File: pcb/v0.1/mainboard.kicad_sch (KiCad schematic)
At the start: 9 parts, among them J1 Conn_01x02_Pin, J2 TYPE_C_Receptacle, J3 Conn_01x04_Pin, U1 AP2112K-3.3TRG1

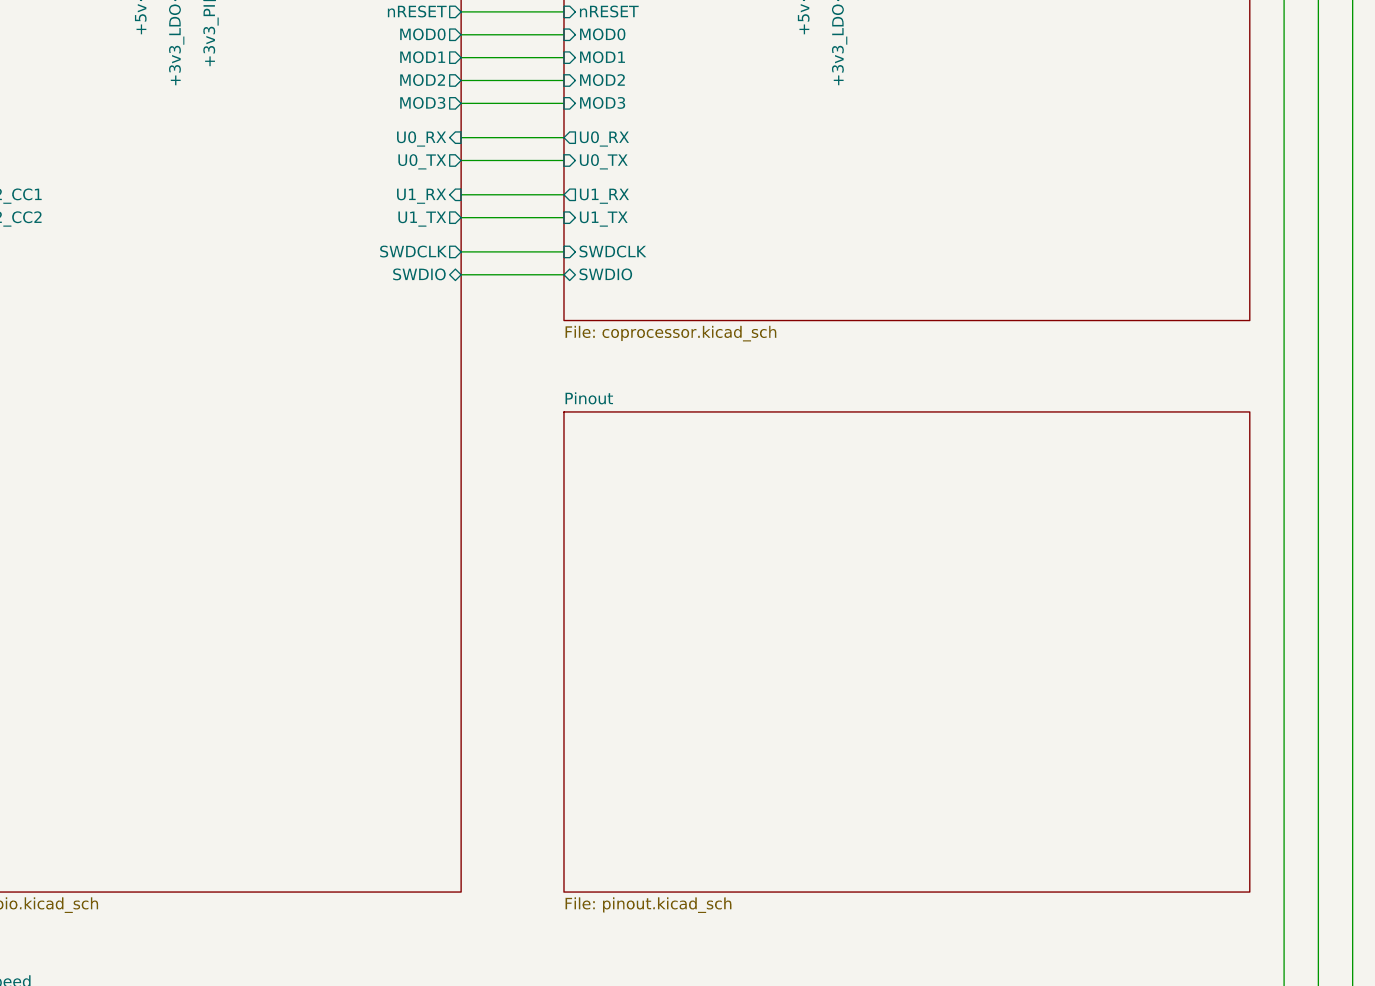
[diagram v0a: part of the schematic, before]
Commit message: Pinout for CM5 and co processor.
I've tried to make the pinout expose as many different protocols as
possible. Standard GPIO exists, but it was not a priority as I think its
more important to have protocols for the backpack.

The co processor also has 8 pins tied as input only. These are
technically I/O, but they have a resistor on them which may mess up some
output operations.
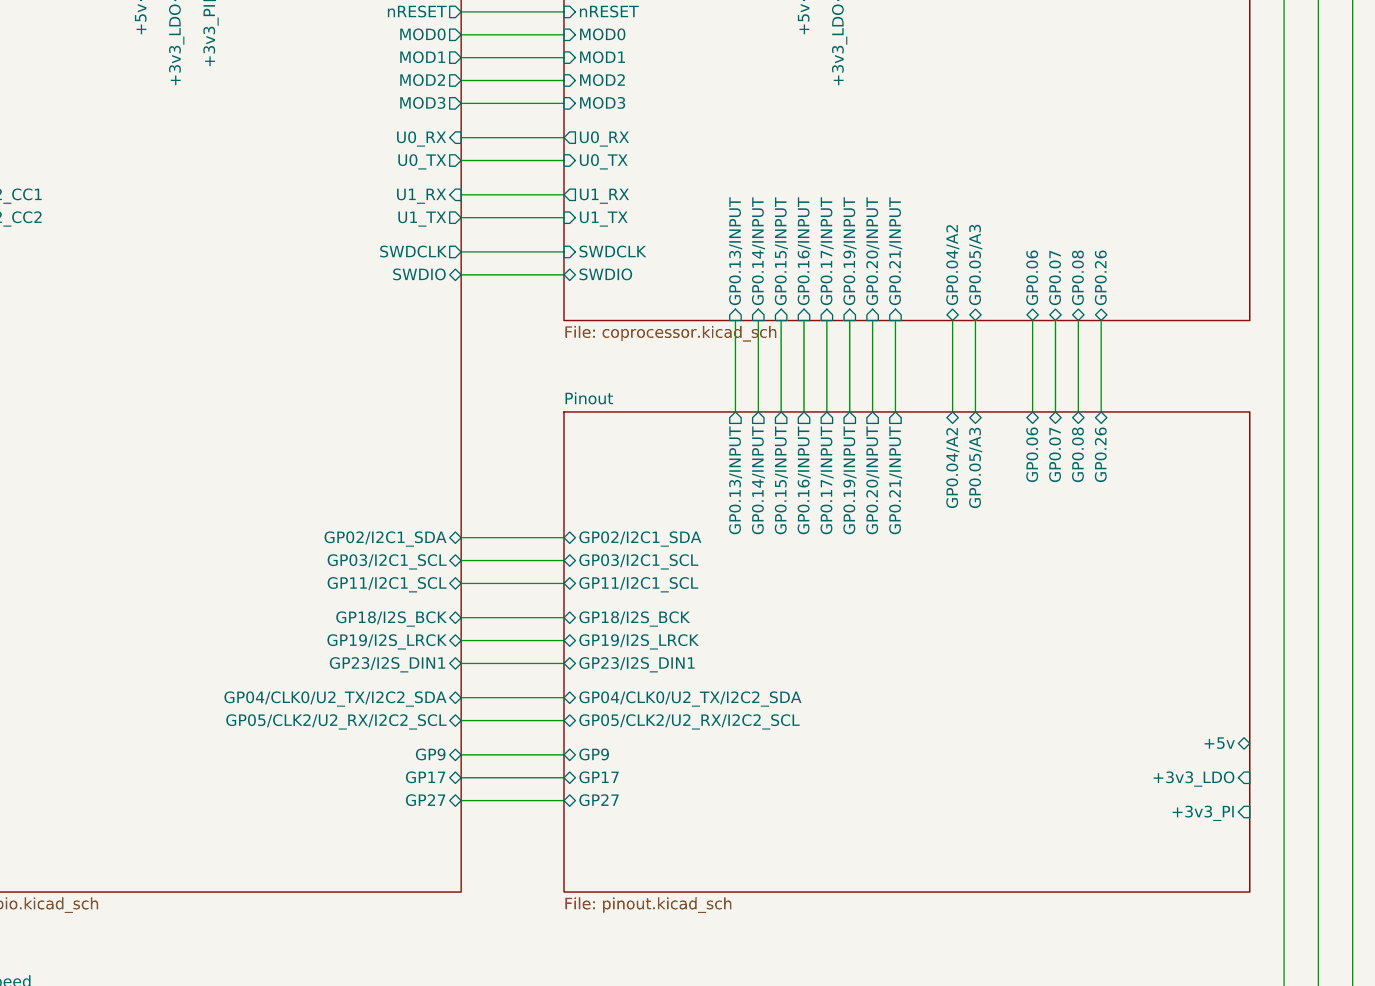
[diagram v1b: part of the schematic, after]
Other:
- sheet Co processor ports: added GP0.04/A2, GP0.05/A3, GP0.06, GP0.07, GP0.08, GP0.13/INPUT, GP0.14/INPUT, GP0.15/INPUT, GP0.16/INPUT, GP0.17/INPUT, GP0.19/INPUT, GP0.20/INPUT, GP0.21/INPUT, GP0.26; removed none
- sheet GPIO ports: added GP02/I2C1_SDA, GP03/I2C1_SCL, GP04/CLK0/U2_TX/I2C2_SDA, GP05/CLK2/U2_RX/I2C2_SCL, GP11/I2C1_SCL, GP17, GP18/I2S_BCK, GP19/I2S_LRCK, GP23/I2S_DIN1, GP27, GP9; removed none
- sheet Pinout ports: added +3v3_LDO, +3v3_PI, +5v, GP0.04/A2, GP0.05/A3, GP0.06, GP0.07, GP0.08, GP0.13/INPUT, GP0.14/INPUT, GP0.15/INPUT, GP0.16/INPUT, GP0.17/INPUT, GP0.19/INPUT, GP0.20/INPUT, GP0.21/INPUT, GP0.26, GP02/I2C1_SDA, GP03/I2C1_SCL, GP04/CLK0/U2_TX/I2C2_SDA, GP05/CLK2/U2_RX/I2C2_SCL, GP11/I2C1_SCL, GP17, GP18/I2S_BCK, GP19/I2S_LRCK, GP23/I2S_DIN1, GP27, GP9; removed none

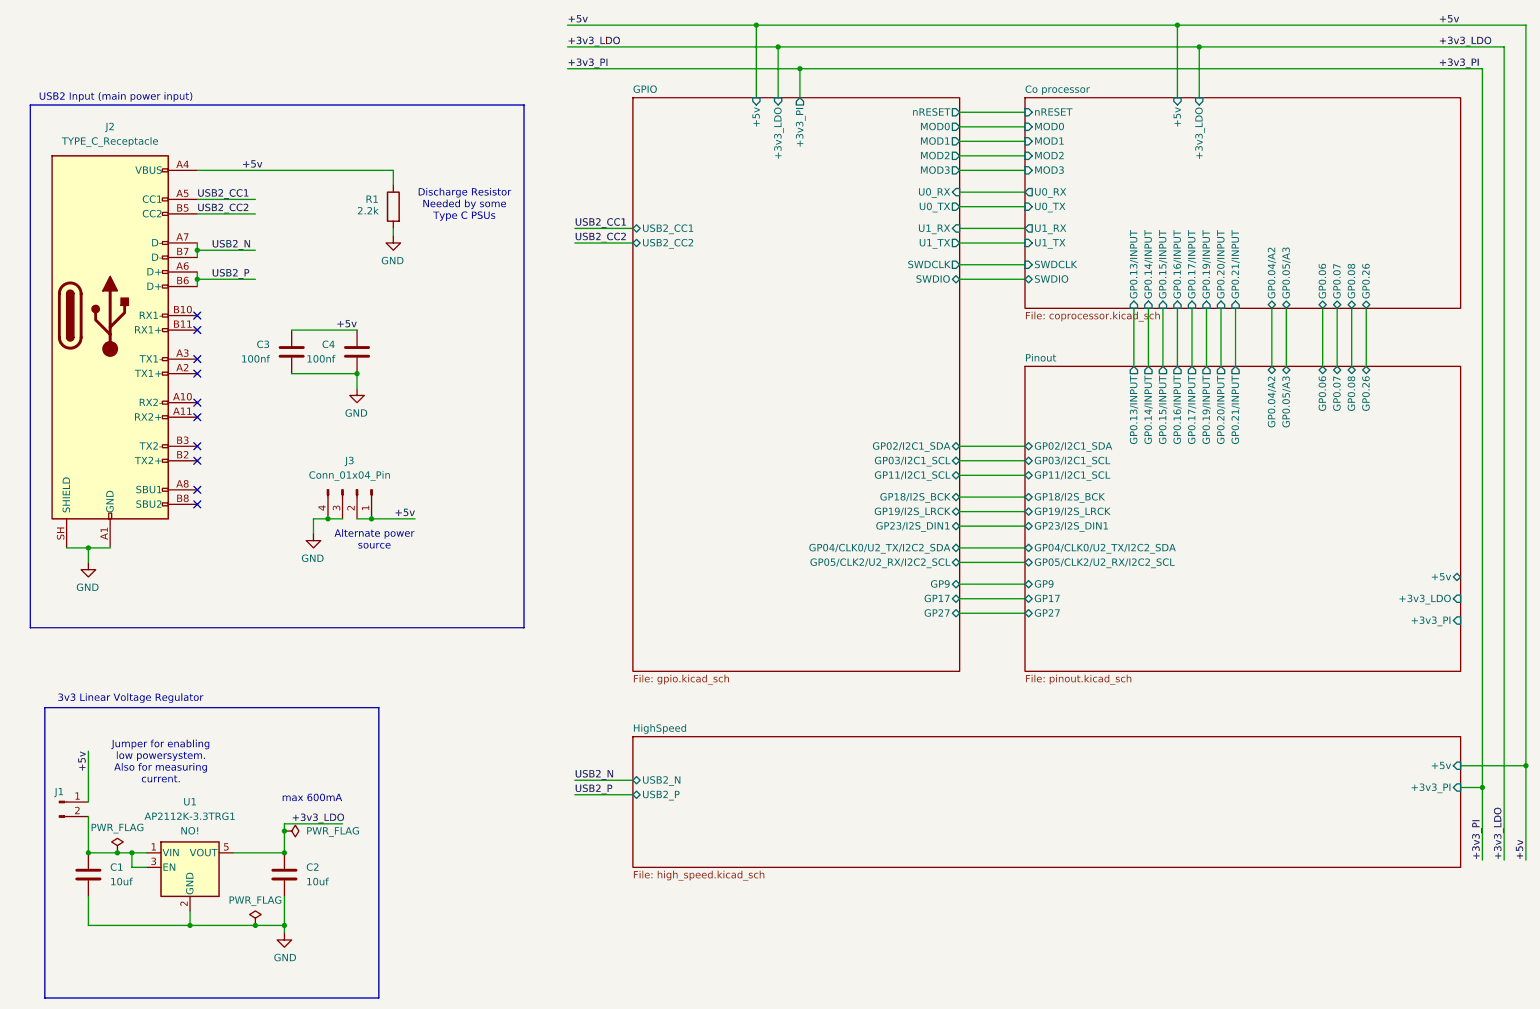
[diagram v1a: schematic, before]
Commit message: Fix display connector wiring
Was not linked up with the i2c and CAM_GPIO pins from the gpio page.
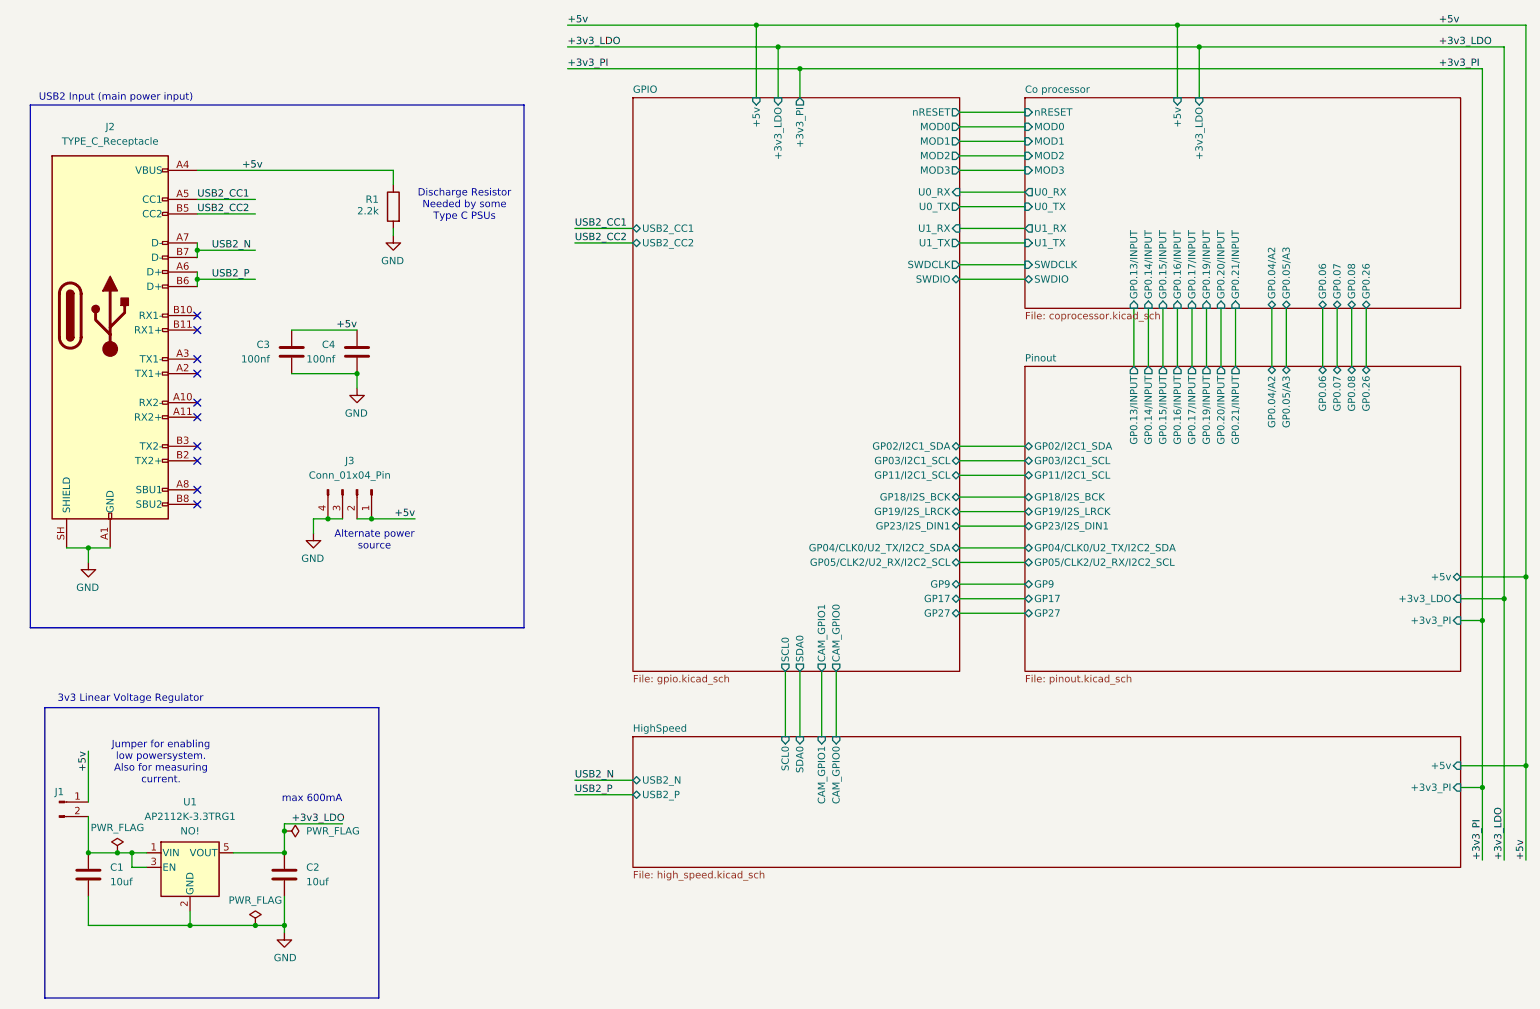
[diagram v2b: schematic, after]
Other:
- sheet GPIO ports: added CAM_GPIO0, CAM_GPIO1, SCL0, SDA0; removed none
- sheet HighSpeed ports: added CAM_GPIO0, CAM_GPIO1, SCL0, SDA0; removed none
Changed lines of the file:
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@@
 	)
 	(junction
+		(at 278.13 115.57)
+		(diameter 0)
+		(color 0 0 0 0)
+	)
+	(junction
 		(at 72.39 101.6)
 		(diameter 0)
@@
 		(color 0 0 0 0)
 	)
+	(junction
+		(at 274.32 119.38)
+		(diameter 0)
+		(color 0 0 0 0)
+	)
+	(junction
+		(at 281.94 111.76)
+		(diameter 0)
+		(color 0 0 0 0)
+	)
 	(no_connect
 		(at 49.53 88.9)
@@
 	(wire
 		(pts
-			(xy 274.32 22.86) (xy 274.32 148.59)
+			(xy 274.32 22.86) (xy 274.32 119.38)
 		)
 		(stroke
@@
 	(wire
 		(pts
+			(xy 270.51 111.76) (xy 281.94 111.76)
+		)
+		(stroke
+			(width 0)
+			(type default)
+		)
+	)
+	(wire
+		(pts
 			(xy 182.88 118.11) (xy 194.31 118.11)
 		)
@@
 	(wire
 		(pts
+			(xy 274.32 119.38) (xy 274.32 148.59)
+		)
+		(stroke
+			(width 0)
+			(type default)
+		)
+	)
+	(wire
+		(pts
 			(xy 182.88 38.1) (xy 194.31 38.1)
 		)
@@
 	(wire
 		(pts
-			(xy 281.94 15.24) (xy 281.94 144.78)
+			(xy 152.4 128.27) (xy 152.4 139.7)
+		)
+		(stroke
+			(width 0)
+			(type default)
+		)
+	)
+	(wire
+		(pts
+			(xy 281.94 15.24) (xy 281.94 111.76)
 		)
 		(stroke
@@
 	(wire
 		(pts
+			(xy 281.94 111.76) (xy 281.94 144.78)
+		)
+		(stroke
+			(width 0)
+			(type default)
+		)
+	)
+	(wire
+		(pts
 			(xy 83.82 40.64) (xy 83.82 43.18)
 		)
@@
 	(wire
 		(pts
+			(xy 278.13 115.57) (xy 278.13 161.29)
+		)
+		(stroke
+			(width 0)
+			(type default)
+		)
+	)
+	(wire
+		(pts
 			(xy 114.3 15.24) (xy 147.32 15.24)
 		)
@@
 	(wire
 		(pts
+			(xy 158.75 128.27) (xy 158.75 139.7)
+		)
+		(stroke
+			(width 0)
+			(type default)
+		)
+	)
+	(wire
+		(pts
 			(xy 147.32 15.24) (xy 147.32 27.94)
 		)
@@
 	(wire
 		(pts
+			(xy 270.51 119.38) (xy 274.32 119.38)
+		)
+		(stroke
+			(width 0)
+			(type default)
+		)
+	)
+	(wire
+		(pts
 			(xy 251.46 64.77) (xy 251.46 74.93)
 		)
@@
 	(wire
 		(pts
+			(xy 270.51 115.57) (xy 278.13 115.57)
+		)
+		(stroke
+			(width 0)
+			(type default)
+		)
+	)
+	(wire
+		(pts
 			(xy 281.94 144.78) (xy 281.94 161.29)
 		)
@@
 	(wire
 		(pts
-			(xy 278.13 19.05) (xy 278.13 161.29)
+			(xy 278.13 19.05) (xy 278.13 115.57)
 		)
 		(stroke
@@
 	(wire
 		(pts
+			(xy 161.29 128.27) (xy 161.29 139.7)
+		)
+		(stroke
+			(width 0)
+			(type default)
+		)
+	)
+	(wire
+		(pts
 			(xy 224.79 19.05) (xy 278.13 19.05)
 		)
@@
 	(wire
 		(pts
+			(xy 154.94 128.27) (xy 154.94 139.7)
+		)
+		(stroke
+			(width 0)
+			(type default)
+		)
+	)
+	(wire
+		(pts
 			(xy 30.48 160.02) (xy 35.56 160.02)
 		)
@@
 			)
 		)
+		(pin "SDA0" output
+			(at 154.94 128.27 270)
+			(effects
+				(font
+					(size 1.27 1.27)
+				)
+				(justify left)
+			)
+		)
+		(pin "SCL0" output
+			(at 152.4 128.27 270)
+			(effects
+				(font
+					(size 1.27 1.27)
+				)
+				(justify left)
+			)
+		)
+		(pin "CAM_GPIO1" output
+			(at 158.75 128.27 270)
+			(effects
+				(font
+					(size 1.27 1.27)
+				)
+				(justify left)
+			)
+		)
+		(pin "CAM_GPIO0" output
+			(at 161.29 128.27 270)
+			(effects
+				(font
+					(size 1.27 1.27)
+				)
+				(justify left)
+			)
+		)
 		(instances
 			(project "mainboard"
@@
 			)
 		)
+		(pin "SCL0" input
+			(at 152.4 139.7 90)
+			(effects
+				(font
+					(size 1.27 1.27)
+				)
+				(justify right)
+			)
+		)
+		(pin "SDA0" input
+			(at 154.94 139.7 90)
+			(effects
+				(font
+					(size 1.27 1.27)
+				)
+				(justify right)
+			)
+		)
+		(pin "CAM_GPIO0" input
+			(at 161.29 139.7 90)
+			(effects
+				(font
+					(size 1.27 1.27)
+				)
+				(justify right)
+			)
+		)
+		(pin "CAM_GPIO1" input
+			(at 158.75 139.7 90)
+			(effects
+				(font
+					(size 1.27 1.27)
+				)
+				(justify right)
+			)
+		)

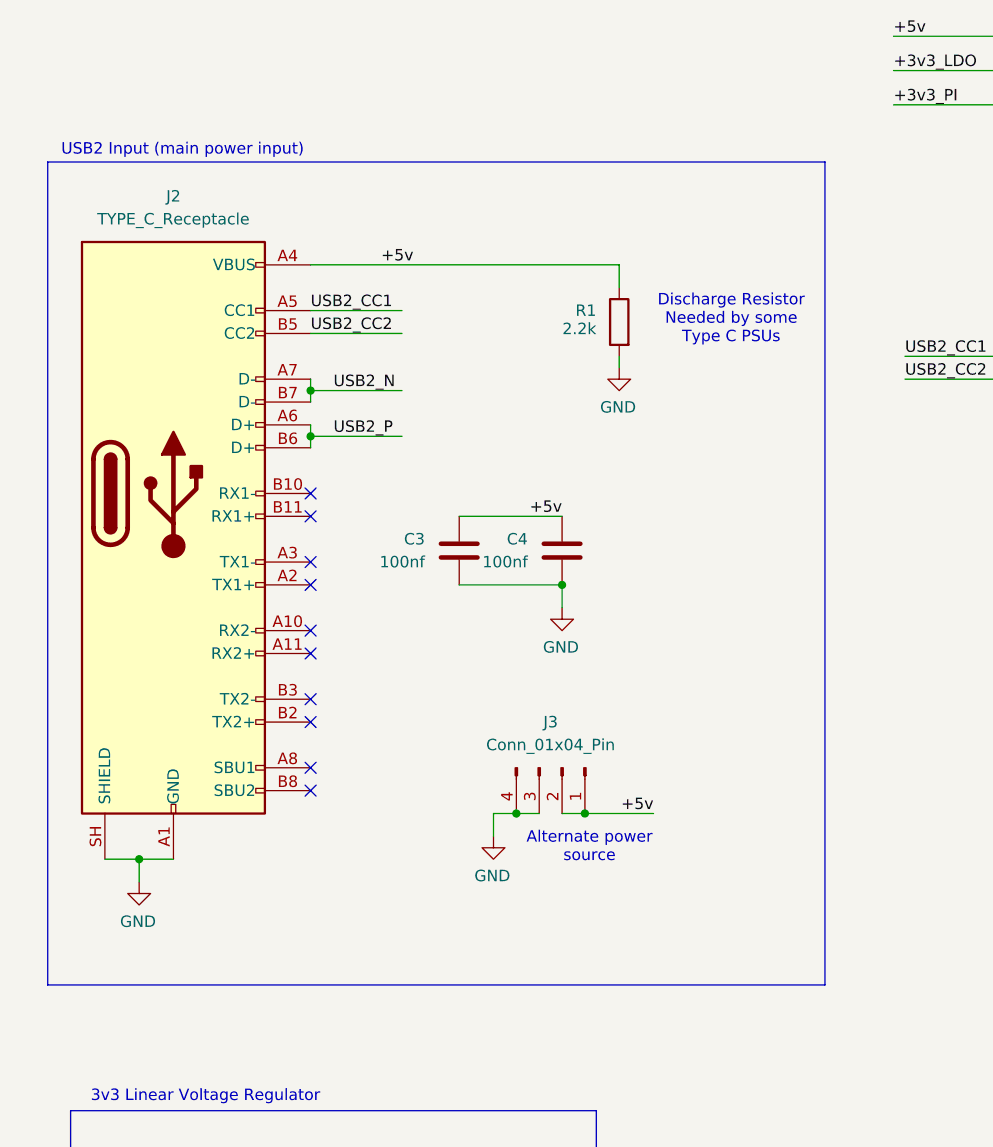
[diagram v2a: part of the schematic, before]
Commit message: High speed and Super speed ESD arrays
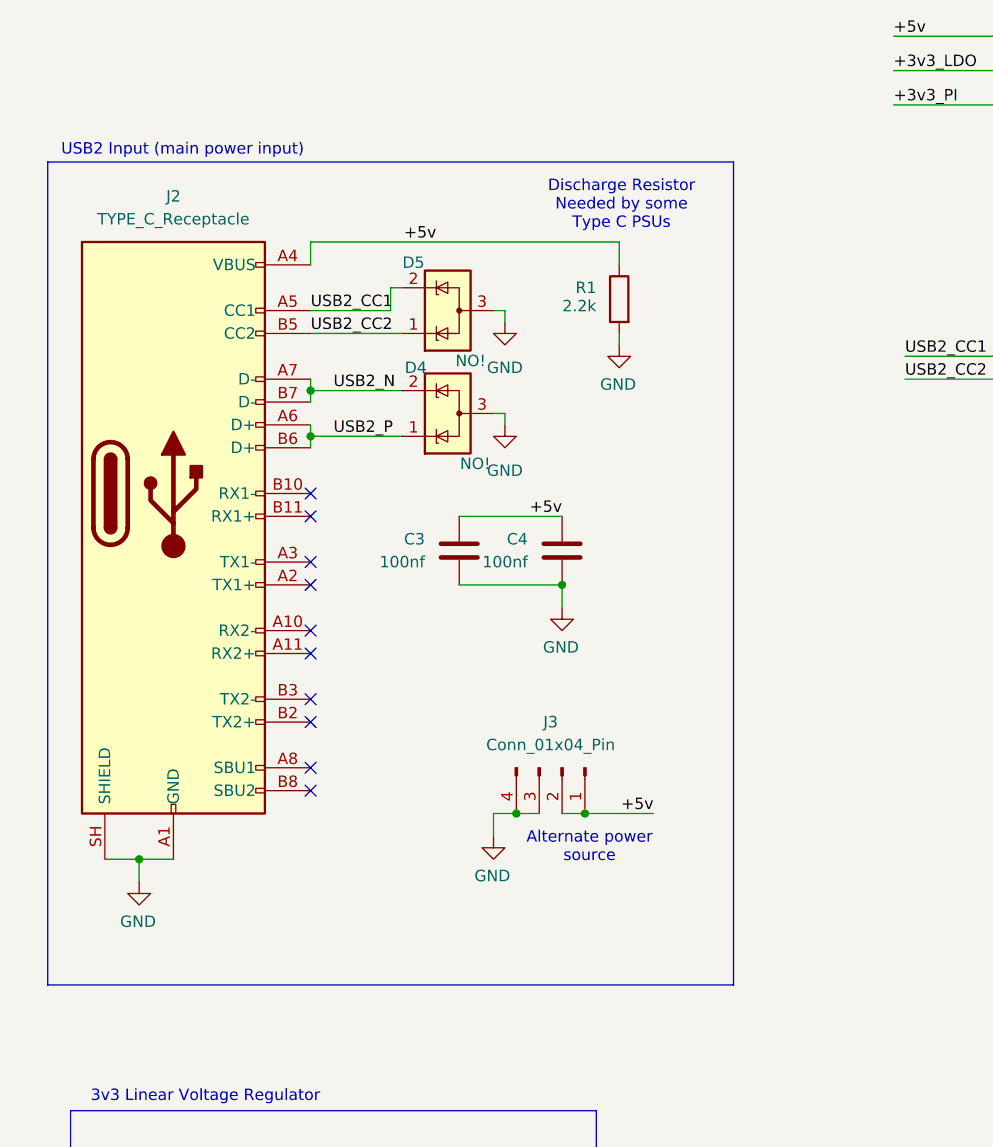
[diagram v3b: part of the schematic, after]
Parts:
- added D4, D5: TECH REPUBLIC ESD5302F, Package_TO_SOT_SMD:SOT-23, symbol TH-1-CC:High_speed_TVS_array
- R1: Stock (none) -> NO!
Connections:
- net GND: now also D4.3 (GND), D5.3 (GND)
- net USB2_CC1: now also D5.2 (IO2)
- net USB2_CC2: now also D5.1 (IO1)
- net USB2_N: now also D4.2 (IO2)
- net USB2_P: now also D4.1 (IO1)
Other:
- moved on the sheet: R1
